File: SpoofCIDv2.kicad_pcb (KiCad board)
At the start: 2 copper layers, 52.8 x 37.2 mm, 28 parts, among them J1 Micro_SD_Card, J2 Conn_01x08, J3 Conn_01x04_Pin, J4 Conn_01x03_Pin, J5 Conn_01x05_Pin, J6 Conn_01x02_Pin, U1 TS3A27518EPW, U2 CY8C4245LQI-483, U3 TVS0500DRV

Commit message: Modified PCB final version
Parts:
- removed U2: CY8C4245LQI-483, Package_DFN_QFN:QFN-40-1EP_6x6mm_P0.5mm_EP4.6x4.6mm
- added C8: 0.1u, Capacitor_SMD:C_0402_1005Metric, F.Cu at (66.0, 75.0)
- added U4: ~, Package_QFP:TQFP-44_10x10mm_P0.8mm, F.Cu at (64.4, 67.2)
- moved J3 13.7 mm to (55.0, 74.5)
- moved J5 13.6 mm to (55.0, 87.5)
- moved J4 13.6 mm to (71.5, 87.5)
- moved D2 6.24 mm to (78.0, 71.5)
- moved R2 6.24 mm to (75.5, 71.5)
- moved D1 6.24 mm to (78.0, 72.6)
- moved R1 6.24 mm to (75.5, 72.6)
- moved C3 1.36 mm to (70.5, 61.0), turned to 90 degrees
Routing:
- net +3.3V: track 88.6 -> 139.7 mm, vias 7 -> 10
- net GND: track 24.8 -> 10.2 mm, vias 30 -> 31
- net /XRESET: track 21.4 -> 33.6 mm
- net /UART_RX: track 9.72 -> 17.7 mm
- net Net-(J5-Pin_5): track 8.00 -> 15.7 mm
- net /UART_TX: track 11.7 -> 19.3 mm
- net Net-(U4-P2.4): track 20.5 -> 28.0 mm
- net Net-(U4-P2.5): track 25.1 -> 32.5 mm
- net Net-(U4-P2.3): track 20.4 -> 27.3 mm
- net Net-(U4-P2.2): track 11.5 -> 18.4 mm
- net Net-(J5-Pin_4): track 9.10 -> 15.4 mm
- net Net-(J5-Pin_3): track 10.2 -> 16.1 mm
- net /SWDIO: track 12.7 -> 8.38 mm
- net Net-(U4-P2.0): track 4.95 -> 9.29 mm
- net Net-(J5-Pin_2): track 12.2 -> 16.5 mm
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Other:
- board size 52.8 x 37.2 mm -> 52 x 50.5 mm

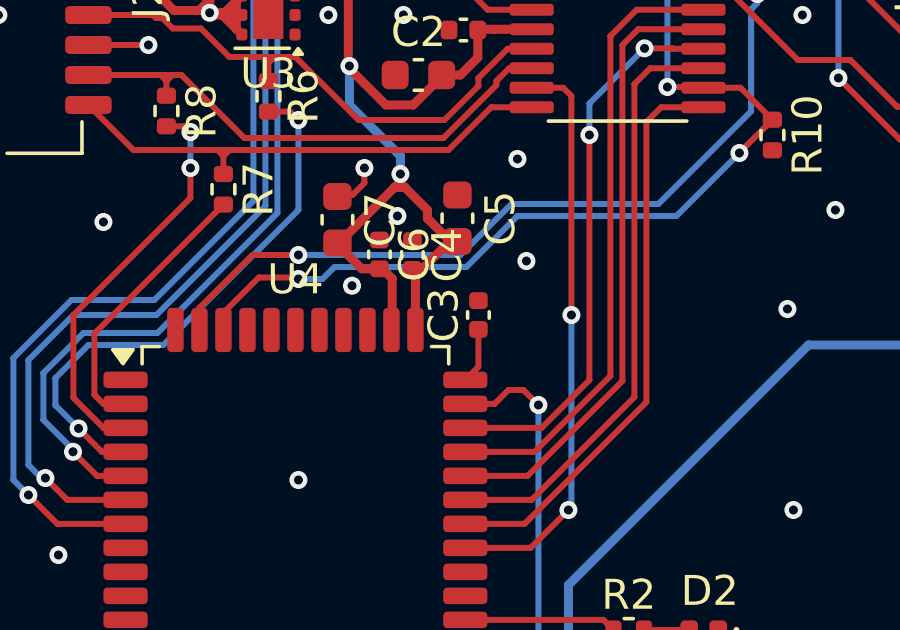
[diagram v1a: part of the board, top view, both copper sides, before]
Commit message: Changed footprint for C3 to Capacitor_SMD:C_0603_1608Metric
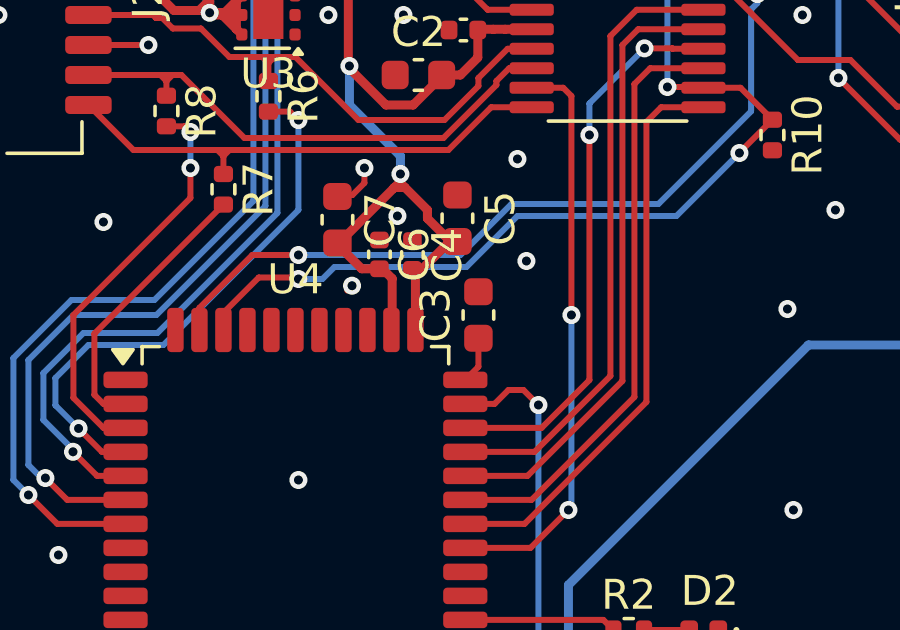
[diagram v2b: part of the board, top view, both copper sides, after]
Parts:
- C3: footprint Capacitor_SMD:C_0402_1005Metric -> Capacitor_SMD:C_0603_1608Metric
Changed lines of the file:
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@@
 		)
 	)
-	(footprint "Capacitor_SMD:C_0402_1005Metric"
+	(footprint "Capacitor_SMD:C_0603_1608Metric"
 		(layer "F.Cu")
 		(at 70.5 61 90)
-		(descr "Capacitor SMD 0402 (1005 Metric), square (rectangular) end terminal, IPC-7351 nominal, (Body size source: IPC-SM-782 page 76, https://www.pcb-3d.com/wordpress/wp-content/uploads/ipc-sm-782a_amendment_1_and_2.pdf), generated with kicad-footprint-generator")
+		(descr "Capacitor SMD 0603 (1608 Metric), square (rectangular) end terminal, IPC-7351 nominal, (Body size source: IPC-SM-782 page 76, https://www.pcb-3d.com/wordpress/wp-content/uploads/ipc-sm-782a_amendment_1_and_2.pdf), generated with kicad-footprint-generator")
 		(tags "capacitor")
 		(property "Reference" "C3"
-			(at 0 -1.16 90)
+			(at 0 -1.43 90)
 			(layer "F.SilkS")
 			(effects
@@
 		)
 		(property "Value" "1.5u"
-			(at 0 1.16 90)
+			(at 0 1.43 90)
 			(layer "F.Fab")
 			(effects
@@
 			)
 		)
-		(property "Datasheet" "https://product.tdk.com/system/files/dam/doc/product/capacitor/ceramic/mlcc/catalog/mlcc_commercial_general_en.pdf"
+		(property "Datasheet" ""
 			(at 0 0 90)
 			(layer "F.Fab")
@@
 			)
 		)
-		(property "Description" "https://www.mouser.es/es/ProductDetail/TDK/C1005X5R1C155K050BC?qs=xLDY6iXSiQY59ZJMhfhKuQ%3D%3D"
+		(property "Description" ""
 			(at 0 0 90)
 			(layer "F.Fab")
@@
 		(attr smd)
 		(fp_line
-			(start -0.107836 -0.36)
-			(end 0.107836 -0.36)
+			(start -0.14058 -0.51)
+			(end 0.14058 -0.51)
 			(stroke
 				(width 0.12)
@@
 		)
 		(fp_line
-			(start -0.107836 0.36)
-			(end 0.107836 0.36)
+			(start -0.14058 0.51)
+			(end 0.14058 0.51)
 			(stroke
 				(width 0.12)
@@
 		)
 		(fp_rect
-			(start -0.91 -0.46)
-			(end 0.91 0.46)
+			(start -1.48 -0.73)
+			(end 1.48 0.73)
 			(stroke
 				(width 0.05)
@@
 		)
 		(fp_rect
-			(start -0.5 -0.25)
-			(end 0.5 0.25)
+			(start -0.8 -0.4)
+			(end 0.8 0.4)
 			(stroke
 				(width 0.1)
@@
 			(effects
 				(font
-					(size 0.25 0.25)
-					(thickness 0.04)
+					(size 0.4 0.4)
+					(thickness 0.06)
 				)
 			)
 		)
 		(pad "1" smd roundrect
-			(at -0.48 0 90)
-			(size 0.56 0.62)
+			(at -0.775 0 90)
+			(size 0.9 0.95)
 			(layers "F.Cu" "F.Mask" "F.Paste")
 			(roundrect_rratio 0.25)
@@
 		)
 		(pad "2" smd roundrect
-			(at 0.48 0 90)
-			(size 0.56 0.62)
+			(at 0.775 0 90)
+			(size 0.9 0.95)
 			(layers "F.Cu" "F.Mask" "F.Paste")
 			(roundrect_rratio 0.25)
 			(net 28 "GND")
 			(pintype "passive")
-			(zone_connect 2)
 		)
 		(embedded_fonts no)
-		(model "${KICAD9_3DMODEL_DIR}/Capacitor_SMD.3dshapes/C_0402_1005Metric.step"
+		(model "${KICAD9_3DMODEL_DIR}/Capacitor_SMD.3dshapes/C_0603_1608Metric.step"
 			(offset
 				(xyz 0 0 0)
